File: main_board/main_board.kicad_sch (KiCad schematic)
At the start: 5 parts, among them U2 FSA3157L6X, U4 FSA3157L6X

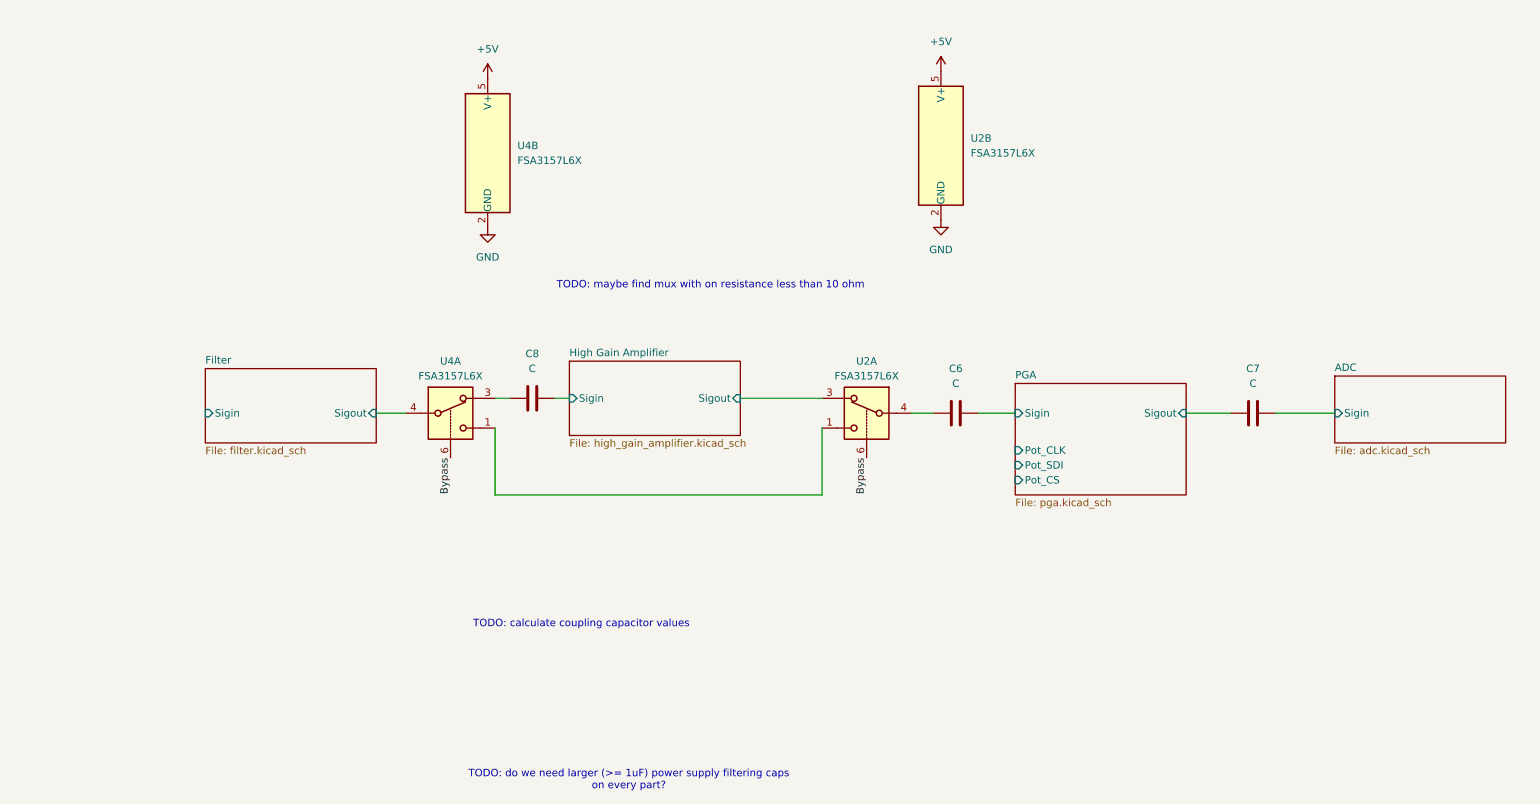
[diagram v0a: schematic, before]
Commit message: switch out mux for non-obsolete part
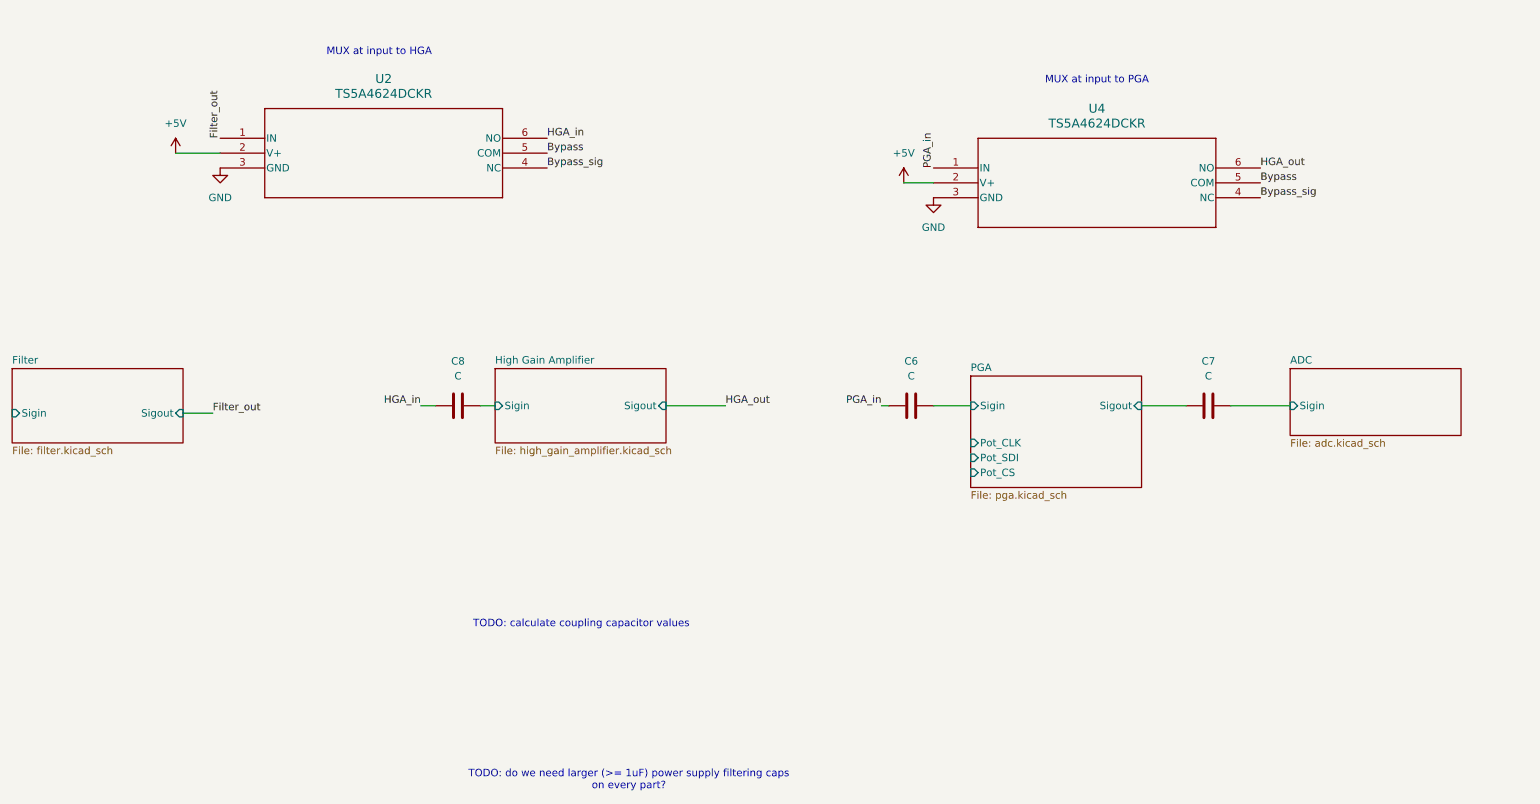
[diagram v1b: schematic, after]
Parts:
- removed U2, U4: FSA3157L6X, Package_SON:Fairchild_MicroPak-6_1.0x1.45mm_P0.5mm, symbol Analog_Switch:FSA3157L6X
- added U2, U4: TS5A4624DCKR, DCK6, symbol Mux:TS5A4624DCKR
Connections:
- net +5V: now also U2.2 (V+), U4.2 (V+)
- net Bypass: now also U2.5 (COM), U4.5 (COM)
- net GND: now also U2.3 (GND), U4.3 (GND)
- net PGA_in: now reaches C6.1
- net PGA_in: now also U4.1 (IN)
- net HGA_in: now reaches C8.1
- net HGA_in: now also U2.6 (NO)
- new net Bypass_sig: U2.4 (NC), U4.4 (NC)
- new net Filter_out: U2.1 (IN)
- new net HGA_out: U4.6 (NO)
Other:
- note added: "MUX at input to HGA"
- note added: "MUX at input to PGA"
- note removed: "TODO: maybe find mux with on resistance less than 10 ohm"
- moved on the sheet: C6, C7, C8

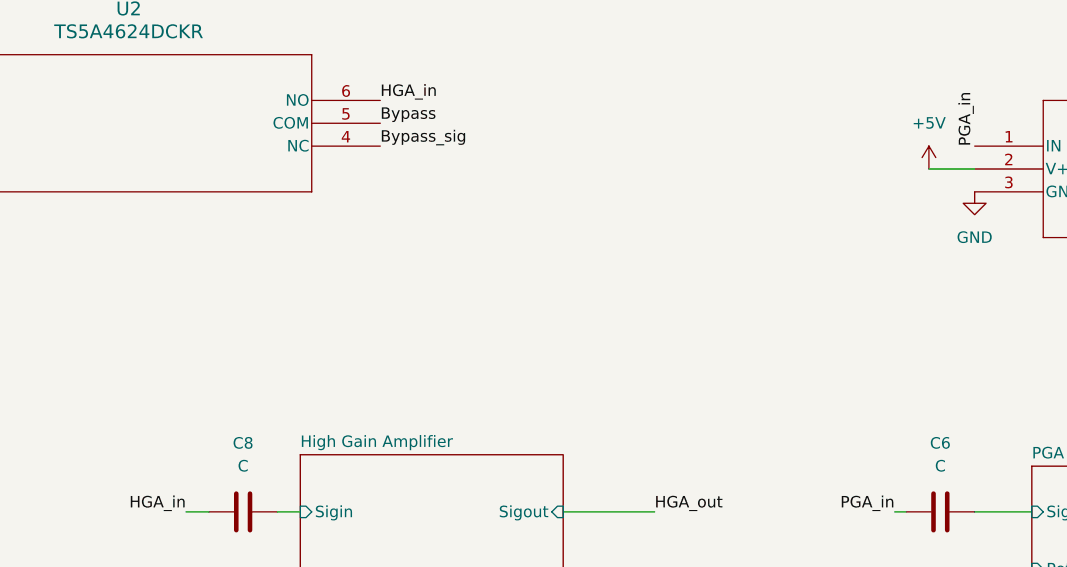
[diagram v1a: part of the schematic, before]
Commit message: add TODO for biasing around muxs
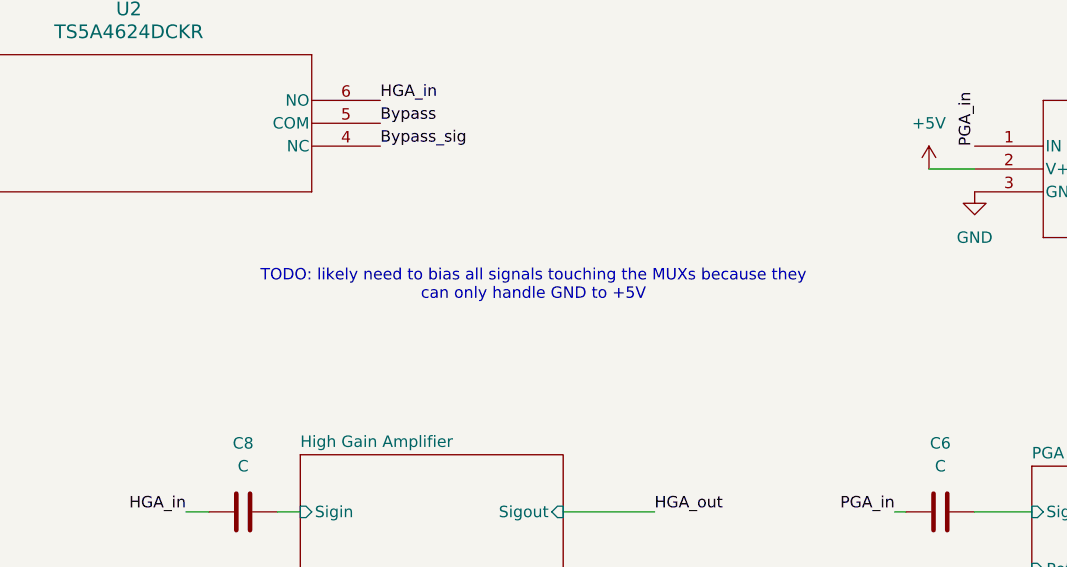
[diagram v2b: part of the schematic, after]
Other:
- note added: "TODO: likely need to bias all signals touching the MUXs because they can only handle GND to +5V"
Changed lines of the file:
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@@
+		)
+	)
+	(text "TODO: likely need to bias all signals touching the MUXs because they \ncan only handle GND to +5V"
+		(exclude_from_sim no)
+		(at 128.778 54.864 0)
+		(effects
+			(font
+				(size 1.27 1.27)
+			)
 		)
 	)

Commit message: update power supply decoupling caps
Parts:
- added C1: 1u, symbol Device:C
- added C15, C19: 100n, symbol Device:C
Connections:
- net +5V: now also C1.1, C15.1, C19.1
- net GND: now also C1.2, C15.2, C19.2
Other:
- note added: "Decoupling caps for MUXs"
- note removed: "TODO: do we need larger (>= 1uF) power supply filtering caps on every part?"

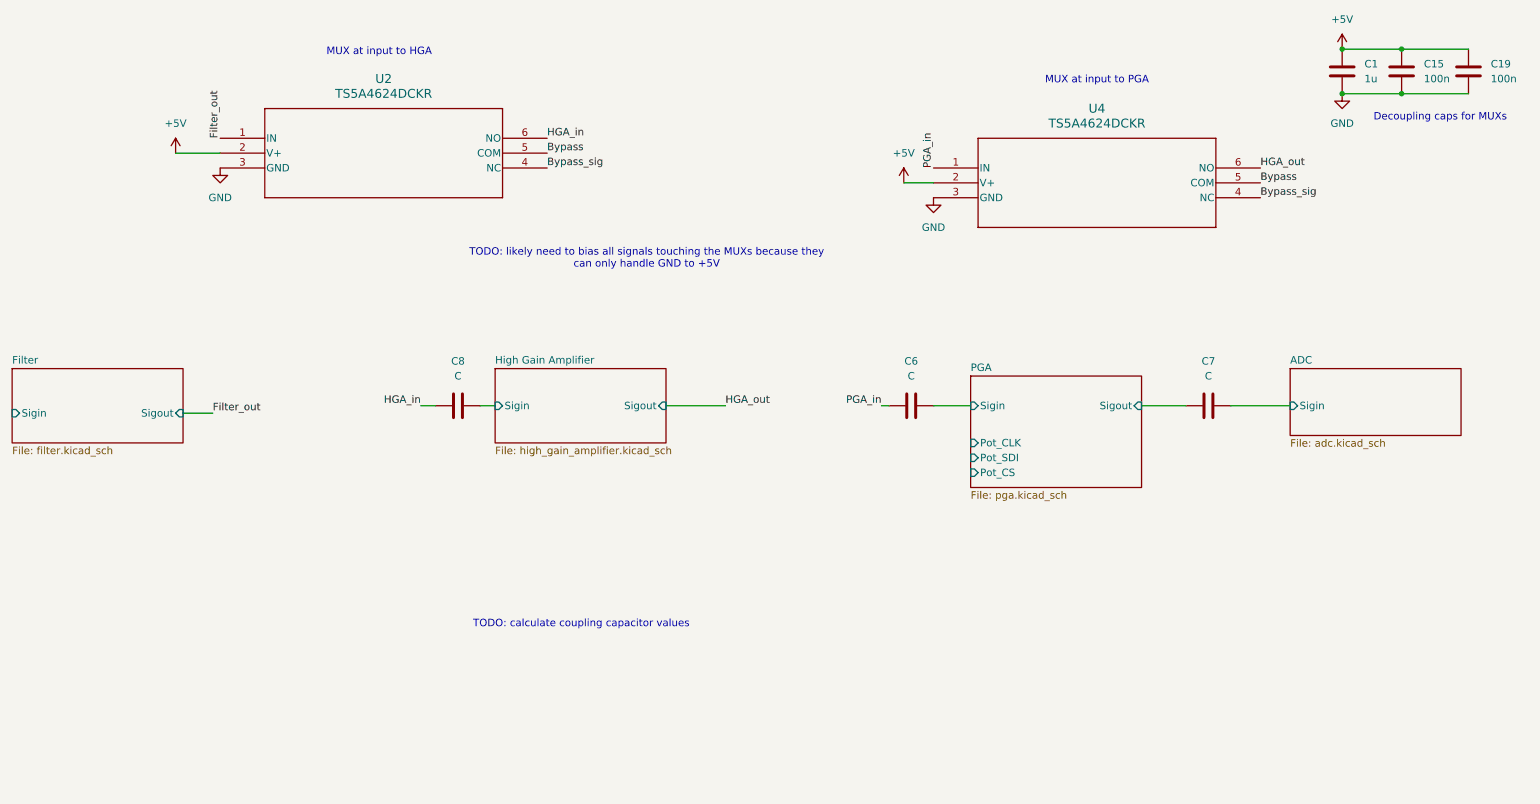
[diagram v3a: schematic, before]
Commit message: Revert "created band pass filter symbol and circuit."
This reverts commit e2b2576e5cedd48076742566f8c9abdfc840a111.

Remove bad commit
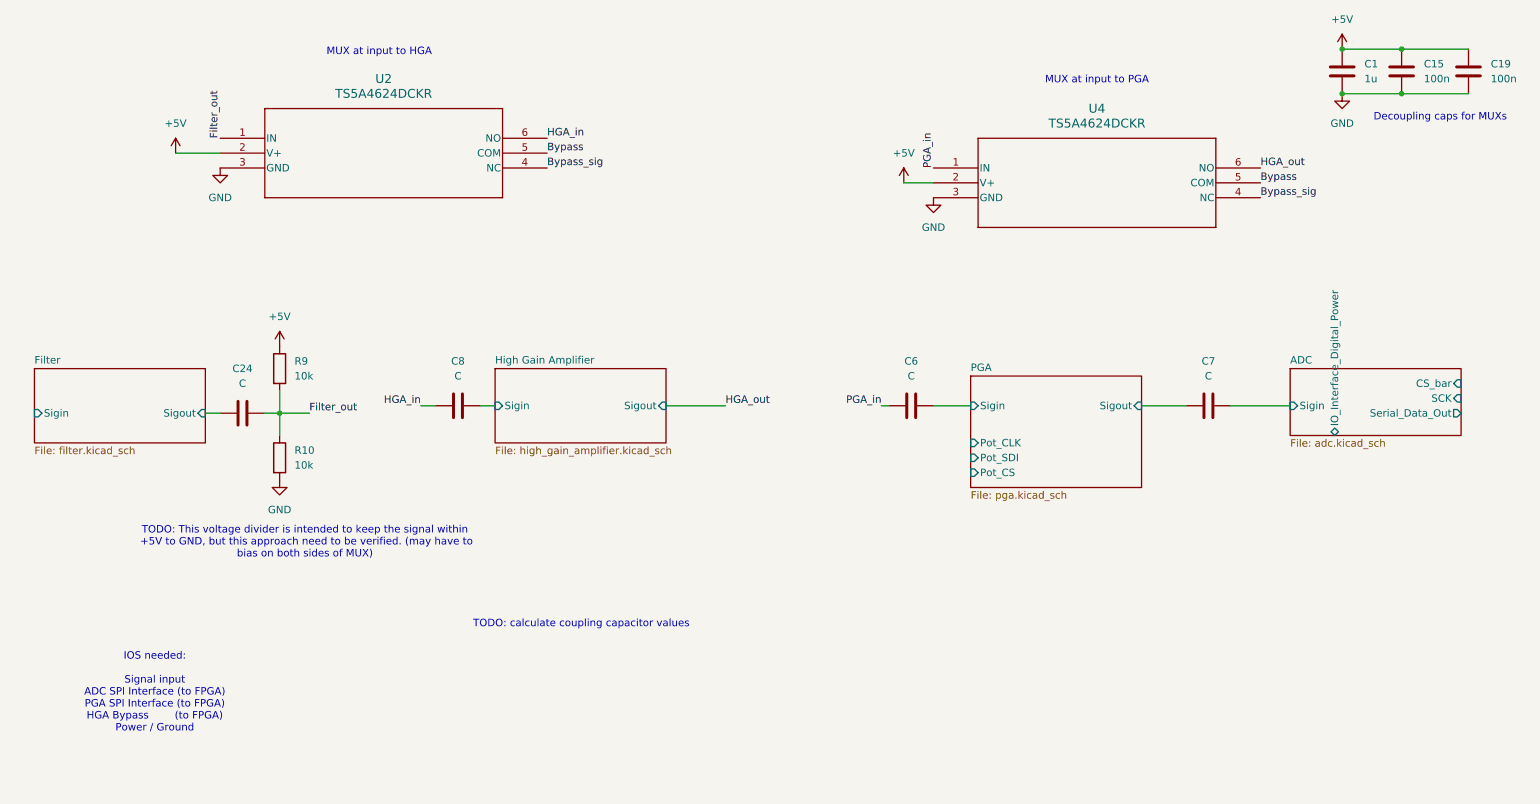
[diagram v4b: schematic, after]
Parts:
- added C24: C, symbol Device:C
- added R10, R9: 10k, symbol Device:R
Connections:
- net +5V: now also R9.1
- net Filter_out: now also C24.2, R10.1, R9.2
- net GND: now also R10.2
- new net Filter/Sigout: C24.1
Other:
- sheet ADC ports: added CS_bar, IO_Interface_Digital_Power, SCK, Serial_Data_Out; removed none
- note added: "IOS needed: Signal input ADC SPI Interface (to FPGA) PGA SPI Interface (to FPGA) HGA Bypass (to FPGA) Power / Ground"
- note added: "TODO: This voltage divider is intended to keep the signal within +5V to GND, but this approach need to be verified. (may have to bias on both sides of MUX)"
- note removed: "TODO: likely need to bias all signals touching the MUXs because they can only handle GND to +5V"

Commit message: created band pass filter symbol and circuit.
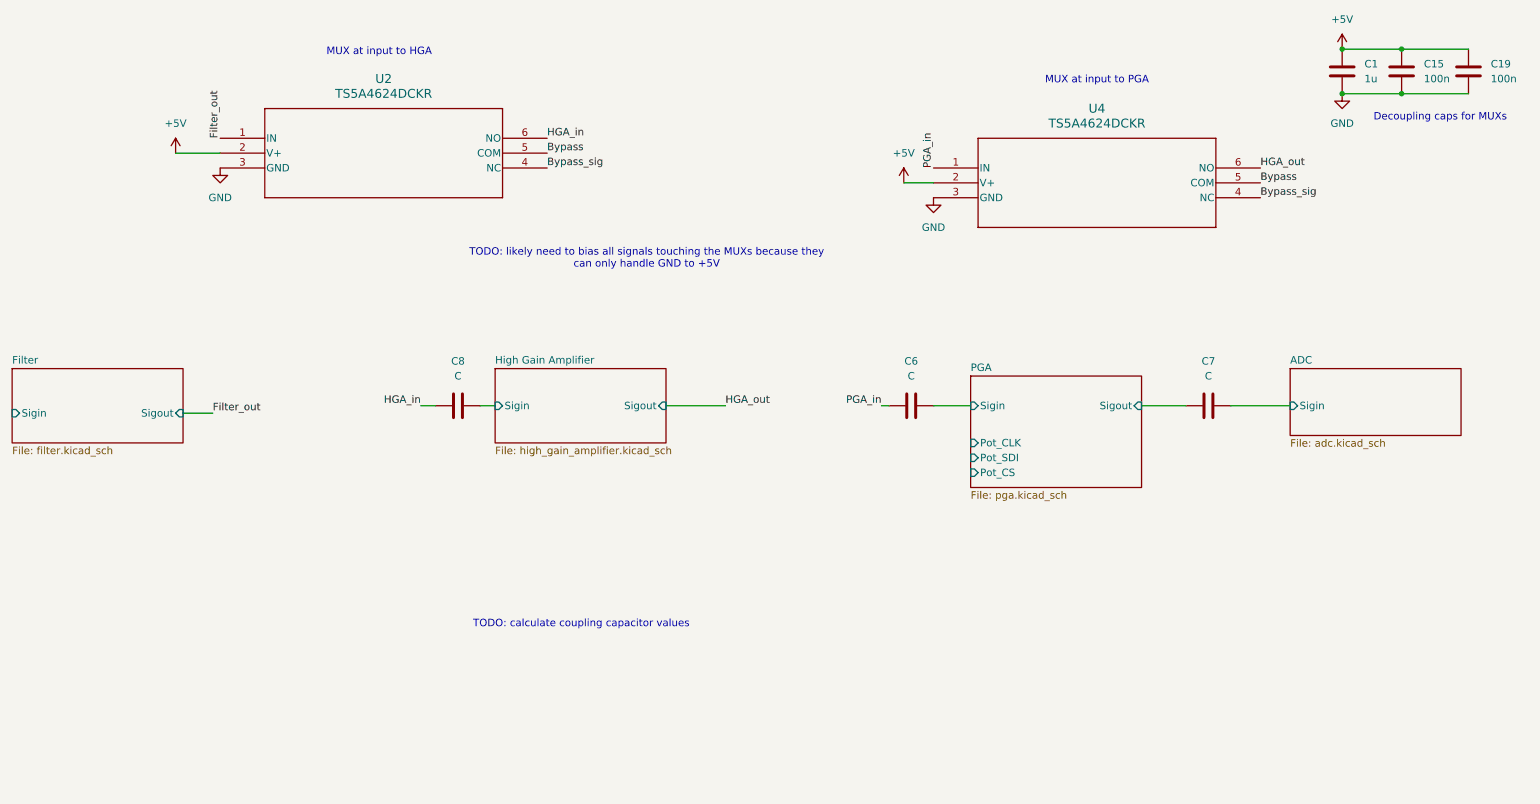
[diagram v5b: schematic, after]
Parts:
- removed C24: C, symbol Device:C
- removed R10, R9: 10k, symbol Device:R
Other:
- sheet ADC ports: added none; removed CS_bar, IO_Interface_Digital_Power, SCK, Serial_Data_Out
- note added: "TODO: likely need to bias all signals touching the MUXs because they can only handle GND to +5V"
- note removed: "IOS needed: Signal input ADC SPI Interface (to FPGA) PGA SPI Interface (to FPGA) HGA Bypass (to FPGA) Power / Ground"
- note removed: "TODO: This voltage divider is intended to keep the signal within +5V to GND, but this approach need to be verified. (may have to bias on both sides of MUX)"

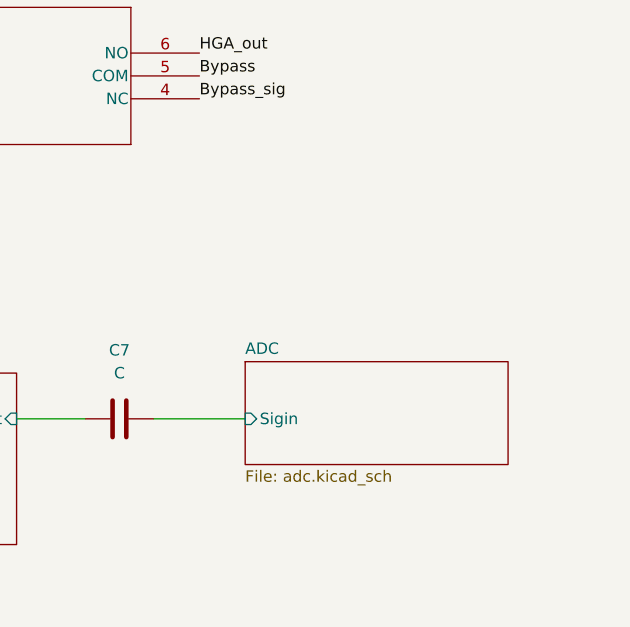
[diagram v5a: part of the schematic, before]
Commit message: sync sheet pins
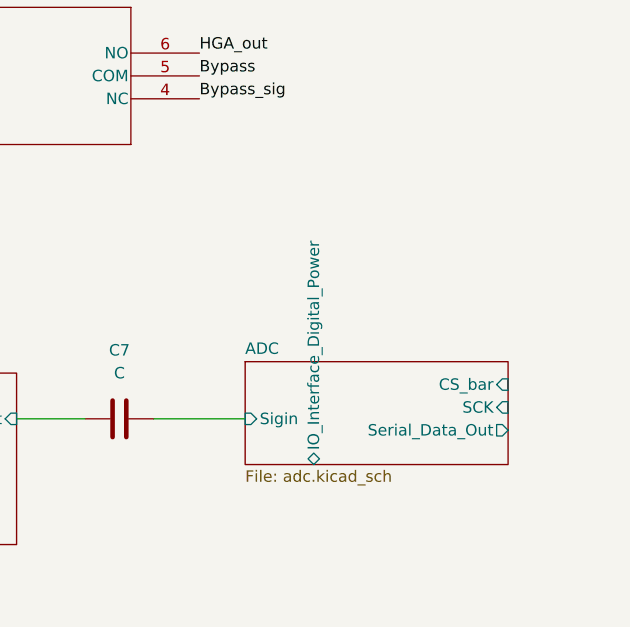
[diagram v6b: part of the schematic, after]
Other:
- sheet ADC ports: added CS_bar, IO_Interface_Digital_Power, SCK, Serial_Data_Out; removed none
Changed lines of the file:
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@@
+			)
+		)
+		(pin "CS_bar" input
+			(at 267.97 76.2 0)
+			(effects
+				(font
+					(size 1.27 1.27)
+				)
+				(justify right)
+			)
+		)
+		(pin "SCK" input
+			(at 267.97 78.74 0)
+			(effects
+				(font
+					(size 1.27 1.27)
+				)
+				(justify right)
+			)
+		)
+		(pin "Serial_Data_Out" output
+			(at 267.97 81.28 0)
+			(effects
+				(font
+					(size 1.27 1.27)
+				)
+				(justify right)
+			)
+		)
+		(pin "IO_Interface_Digital_Power" bidirectional
+			(at 246.38 85.09 270)
+			(effects
+				(font
+					(size 1.27 1.27)
+				)
+				(justify left)
 			)
 		)
